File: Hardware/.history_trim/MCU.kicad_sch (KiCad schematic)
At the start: 33 parts, among them J2 Conn_Coaxial, Q7 BCR116, U5 MS5611, U6 ICM-42688-P, U7 ADXL375, U9 MAX-M10N

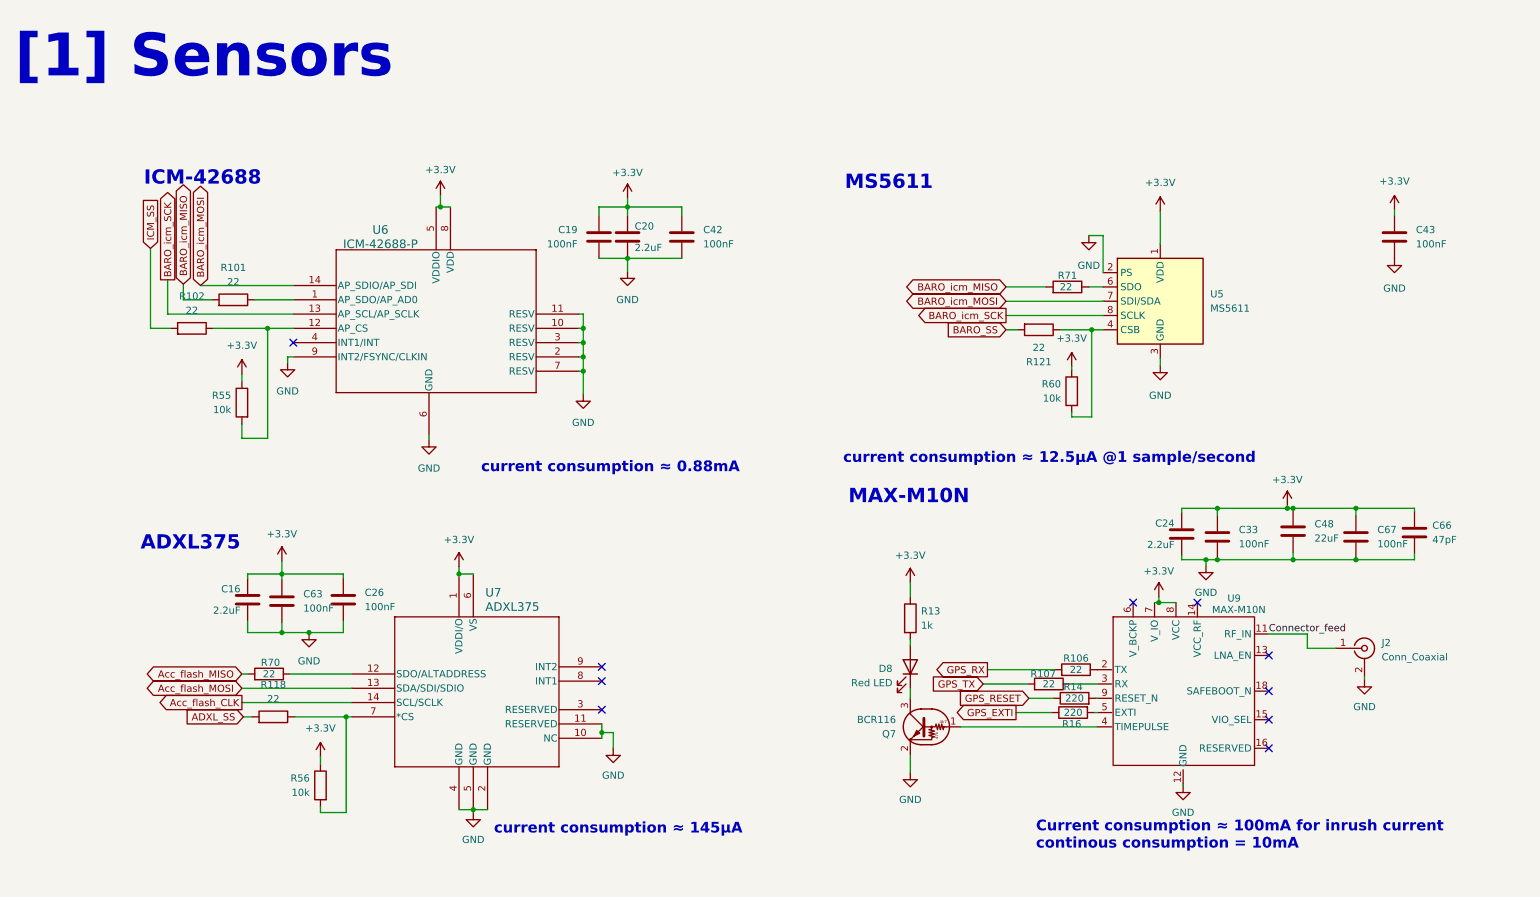
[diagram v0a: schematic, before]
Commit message: Purged heavy binaries and updated gitignore
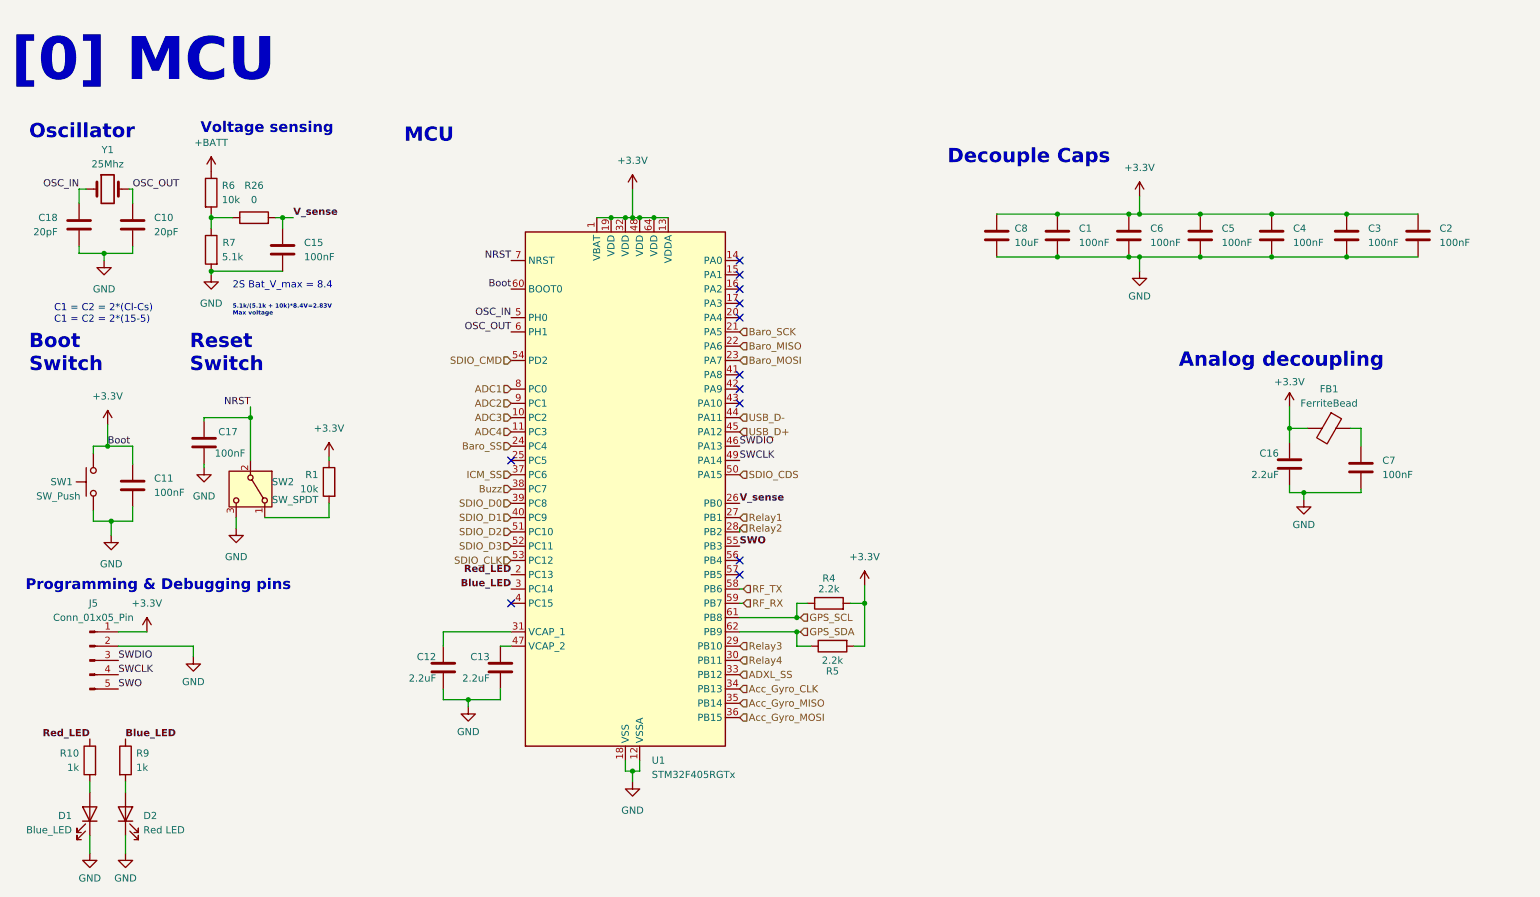
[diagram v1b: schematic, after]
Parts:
- removed C19, C26, C33, C42, C43, C63, C67: 100nF, Capacitor_SMD:C_0603_1608Metric, symbol Device:C
- removed C20, C24: 2.2uF, Capacitor_SMD:C_0603_1608Metric, symbol Device:C
- removed C48: 22uF, Capacitor_SMD:C_0805_2012Metric, symbol Device:C
- removed C66: 47pF, Capacitor_SMD:C_0603_1608Metric, symbol Device:C
- removed D8: Red LED, Capacitor_SMD:C_0603_1608Metric, symbol Device:LED
- removed J2: Conn_Coaxial, Connector_Coaxial:SMA_Amphenol_132134-10_Vertical, symbol Connector:Conn_Coaxial
- removed Q7: BCR116, Package_TO_SOT_SMD:SOT-23-3, symbol Transistor_BJT:DTC143Z
- removed R101, R102, R106, R107, R118, R121, R70, R71: 22, Resistor_SMD:R_0603_1608Metric, symbol Device:R
- removed R13: 1k, Resistor_SMD:R_0603_1608Metric, symbol Device:R
- removed R14, R16: 220, Resistor_SMD:R_0603_1608Metric, symbol Device:R
- removed R55, R56, R60: 10k, Resistor_SMD:R_0603_1608Metric, symbol Device:R
- removed U5: MS5611, MS5611:SON8_MS5611_TEC, symbol Sensor_Pressure:MS5611-01BA
- removed U6: ICM-42688-P, ICM_42688_P:LGA14_2P5X3X0P91_TDK, symbol 2026-06-16_08-50-59:ICM-42688-P
- removed U7: ADXL375, ADXL375BCCZ_RL7:LGA_CC-14-1_ADI-L, symbol 2026-07-20_16-43-50:ADXL375BCCZ-RL7
- removed U9: MAX-M10N, RF_GPS:ublox_MAX, symbol 2026-03-10_07-36-19:MAX-M10N
- added C1, C11, C15, C17, C2, C3, C4, C5, C6, C7: 100nF, Capacitor_SMD:C_0402_1005Metric, symbol Device:C
- added C10, C18: 20pF, Capacitor_SMD:C_0603_1608Metric, symbol Device:C
- added C12, C13: 2.2uF, Capacitor_SMD:C_0402_1005Metric, symbol Device:C
- added C8: 10uF, Capacitor_SMD:C_0805_2012Metric, symbol Device:C
- added D1: Blue_LED, Capacitor_SMD:C_0603_1608Metric, symbol Device:LED
- added D2: Red LED, Capacitor_SMD:C_0603_1608Metric, symbol Device:LED
- added FB1: FerriteBead, symbol Device:FerriteBead
- added J5: Conn_01x05_Pin, symbol Connector:Conn_01x05_Pin
- added R1, R6: 10k, Resistor_SMD:R_0603_1608Metric, symbol Device:R
- added R10, R9: 1k, Resistor_SMD:R_0402_1005Metric, symbol Device:R
- added R26: 0, Resistor_SMD:R_0402_1005Metric, symbol Device:R
- added R4, R5: 2.2k, symbol Device:R
- added R7: 5.1k, Resistor_SMD:R_0402_1005Metric, symbol Device:R
- added SW1: SW_Push, Button_Switch_SMD:SW_SPST_PTS810, symbol Switch:SW_Push
- added SW2: SW_SPDT, Button_Switch_SMD:SW_SPDT_CK_JS102011SAQN, symbol Switch:SW_SPDT
- added U1: STM32F405RGTx, Package_QFP:LQFP-64_10x10mm_P0.5mm, symbol MCU_ST_STM32F4:STM32F405RGTx
- added Y1: 25Mhz, footprints:Custom_Oscillator, symbol Device:Crystal
- C16: footprint Capacitor_SMD:C_0603_1608Metric -> Capacitor_SMD:C_0402_1005Metric; Distributer Link https://www.ozdisan.com/p/smt-smd-ve-mlcc-kapasitorler-184/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 -> http://ozdisan.com/p/smt-smd-ve-mlcc-kapasitorler-184/murat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; Part Number CL10B225KP8NNNC -> GRT155C81A225ME13D
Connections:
- net +3.3V: now also C1.1, C11.1, C2.1, C3.1, C4.1, C5.1, C6.1, C8.1, FB1.2, J5.1 (Pin_1), R1.1, R4.2, R5.2, SW1.2, U1.1 (VBAT), U1.13 (VDDA), U1.19 (VDD), U1.32 (VDD), U1.48 (VDD), U1.60 (BOOT0), U1.64 (VDD)
- net ADXL_SS: now also U1.33 (PB12)
- net GND: now also C1.2, C10.2, C11.2, C12.2, C13.2, C15.2, C17.2, C18.2, C2.2, C3.2, C4.2, C5.2, C6.2, C7.2, C8.2, D1.1 (K), D2.1 (K), J5.2 (Pin_2), R7.2, SW1.1, SW2.3 (C), U1.12 (VSSA), U1.18 (VSS), U1.63 (VSS)
- net ICM_SS: now also U1.37 (PC6)
- new net: C7.1, FB1.1
- new net: D2.2 (A), R9.2
- new net: R1.2, SW2.1 (A)
- new net: R26.1, R6.2, R7.1
- new net: C12.1, U1.31 (VCAP_1)
- new net: C13.1, U1.47 (VCAP_2)
- new net: D1.2 (A), R10.2
- new net +BATT: R6.1
- new net ADC1: U1.8 (PC0)
- new net ADC2: U1.9 (PC1)
- new net ADC3: U1.10 (PC2)
- new net ADC4: U1.11 (PC3)
- new net Acc_Gyro_CLK: U1.34 (PB13)
- new net Acc_Gyro_MISO: U1.35 (PB14)
- new net Acc_Gyro_MOSI: U1.36 (PB15)
- new net Baro_MISO: U1.22 (PA6)
- new net Baro_MOSI: U1.23 (PA7)
- new net Baro_SCK: U1.21 (PA5)
- new net Baro_SS: U1.24 (PC4)
- new net Blue_LED: R9.1, U1.3 (PC14)
- new net Buzz: U1.38 (PC7)
- new net GPS_SCL: R4.1, U1.61 (PB8)
- new net GPS_SDA: R5.1, U1.62 (PB9)
- new net NRST: C17.1, SW2.2 (B), U1.7 (NRST)
- new net OSC_IN: C18.1, U1.5 (PH0), Y1.1
- new net OSC_OUT: C10.1, U1.6 (PH1), Y1.2
- new net RF_RX: U1.59 (PB7)
- new net RF_TX: U1.58 (PB6)
- new net Red_LED: R10.1, U1.2 (PC13)
- new net Relay1: U1.27 (PB1)
- new net Relay2: U1.28 (PB2)
- new net Relay3: U1.29 (PB10)
- new net Relay4: U1.30 (PB11)
- new net SDIO_CDS: U1.50 (PA15)
- new net SDIO_CLK: U1.53 (PC12)
- new net SDIO_CMD: U1.54 (PD2)
- new net SDIO_D0: U1.39 (PC8)
- new net SDIO_D1: U1.40 (PC9)
- new net SDIO_D2: U1.51 (PC10)
- new net SDIO_D3: U1.52 (PC11)
- new net SWCLK: J5.4 (Pin_4), U1.49 (PA14)
- new net SWDIO: J5.3 (Pin_3), U1.46 (PA13)
- new net SWO: J5.5 (Pin_5), U1.55 (PB3)
- new net USB_D+: U1.45 (PA12)
- new net USB_D-: U1.44 (PA11)
- new net V_sense: C15.1, R26.2, U1.26 (PB0)
- no-connect marks 10 -> 12
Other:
- note added: "2S Bat_V_max = 8.4"
- note added: "5.1k/(5.1k + 10k)*8.4V=2.83V Max voltage"
- note added: "Analog decoupling"
- note added: "Boot Switch"
- note added: "C1 = C2 = 2*(Cl-Cs) C1 = C2 = 2*(15-5)"
- note added: "Decouple Caps"
- note added: "MCU"
- note added: "Oscillator"
- note added: "Programming & Debugging pins"
- note added: "Reset Switch"
- note added: "Voltage sensing"
- note added: "[0] MCU"
- note removed: "ADXL375"
- note removed: "Current consumption ≈ 100mA for inrush current continous consumption = 10mA"
- note removed: "ICM-42688"
- note removed: "MAX-M10N"
- note removed: "MS5611"
- note removed: "[1] Sensors"
- note removed: "current consumption ≈ 0.88mA"
- note removed: "current consumption ≈ 12.5µA @1 sample/second"
- note removed: "current consumption ≈ 145µA"
- title: Sensors -> MCU
